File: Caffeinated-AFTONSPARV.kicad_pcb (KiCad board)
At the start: 4 copper layers, 42.5 x 16.1 mm, 37 parts, among them J1 PWR, J2 LED, J3 TagConnect, J4 USB, Q1 AO3400A, Q2 AO3400A, Q3 AO3400A, SW1 SW_Push, U1 ESP32-C3-MINI-1-[H/N]4, U2 SY8201ABC

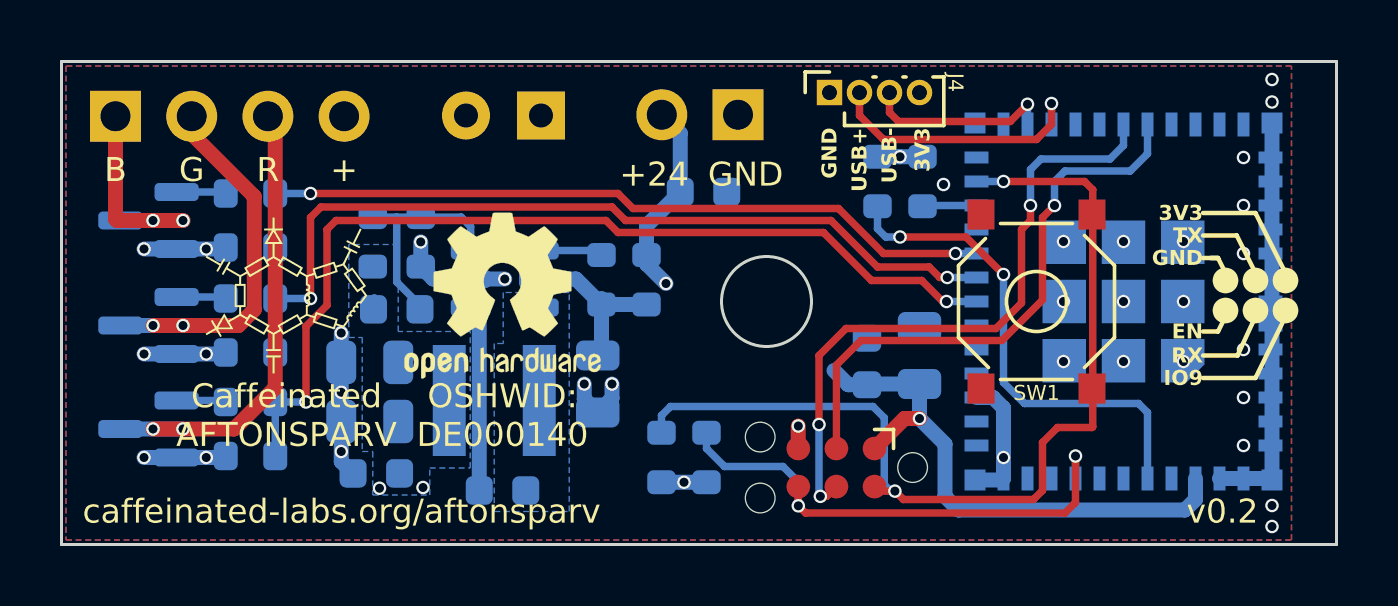
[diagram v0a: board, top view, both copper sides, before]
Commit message: optimize bom for jlcpcb basic parts
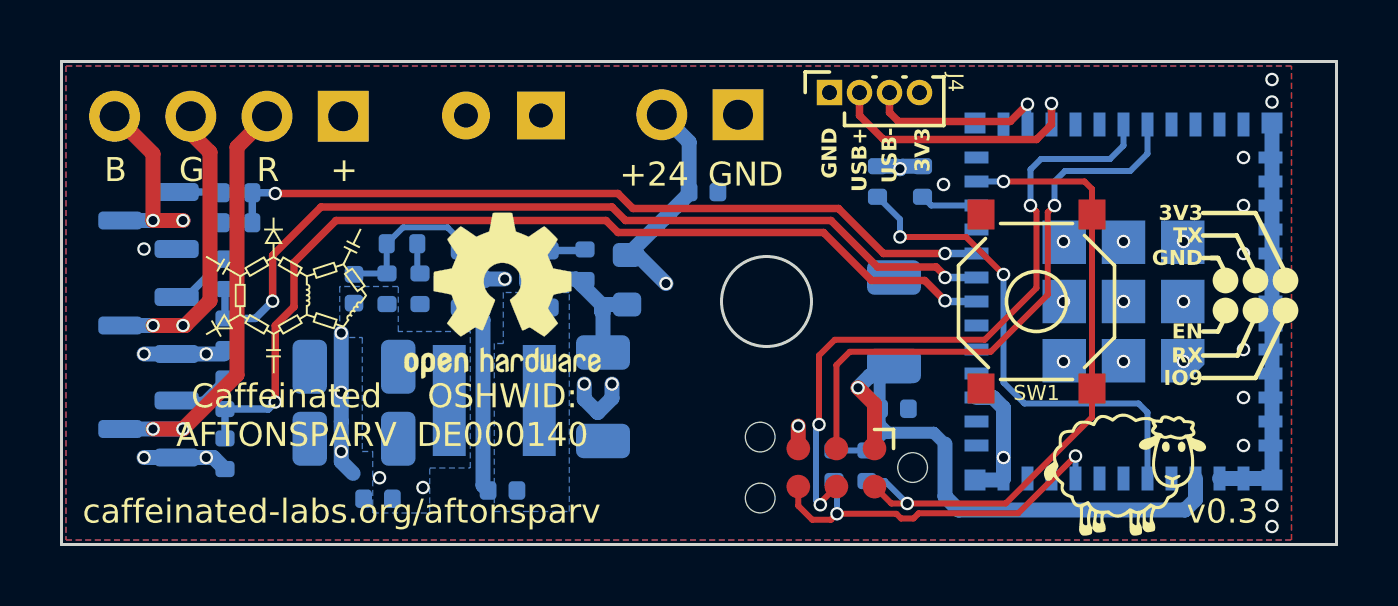
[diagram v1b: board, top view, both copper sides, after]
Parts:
- added R15: 100Ω, Resistor_SMD:R_0402_1005Metric, B.Cu at (141.8, 99.6)
- added sheep: LOGO, LOGO, F.Cu at (165.2, 105.8)
- C1: value 100nF -> 100nF 50V; footprint Capacitor_SMD:C_0603_1608Metric -> Capacitor_SMD:C_0402_1005Metric
- C10, C3, C6, C9: footprint Capacitor_SMD:C_0805_2012Metric -> Capacitor_SMD:C_1206_3216Metric
- C11, C4, C5, C7: footprint Capacitor_SMD:C_0603_1608Metric -> Capacitor_SMD:C_0402_1005Metric
- R1, R10, R12, R14, R2, R3, R7, R8, R9: footprint Resistor_SMD:R_0603_1608Metric -> Resistor_SMD:R_0402_1005Metric
- R13: value 22.1kΩ -> 22kΩ; footprint Resistor_SMD:R_0603_1608Metric -> Resistor_SMD:R_0402_1005Metric
- R4, R5, R6: value 20Ω -> 22Ω; footprint Resistor_SMD:R_0603_1608Metric -> Resistor_SMD:R_0402_1005Metric
- moved J2 7.59 mm to (139.2, 93.8), turned to 90 degrees
- moved R7 6.86 mm to (156.7, 105.5), turned to -90 degrees
- moved R10 4.26 mm to (155.6, 105.5), turned to -90 degrees
- moved C7 1.81 mm to (157.6, 103.6), turned to 0 degrees
- moved R12 1.63 mm to (140.7, 99.6)
- moved C5 1.58 mm to (139.6, 99.6), turned to -90 degrees
- moved C6 1.41 mm to (157.6, 100.7)
- moved R4 1.18 mm to (135.2, 99.1), turned to 90 degrees
- moved R2 1.06 mm to (135.2, 101.1), turned to -90 degrees
- moved R1 0.94 mm to (135.7, 97.4)
- moved R6 0.89 mm to (135.2, 103.1), turned to 90 degrees
- moved R3 0.85 mm to (135.2, 105.1), turned to -90 degrees
- moved C11 0.85 mm to (140.3, 106.6)
- moved C10 0.78 mm to (139.6, 104.6)
- moved R14 0.74 mm to (147.2, 98.8)
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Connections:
- J2 pad 1: Net-(J2-Pin_1) -> +24V
- J2 pad 4: +24V -> Net-(J2-Pin_4)
- Q1 pad 3: Net-(J2-Pin_3) -> Net-(J2-Pin_2)
- Q2 pad 3: Net-(J2-Pin_2) -> Net-(J2-Pin_3)
- Q3 pad 3: Net-(J2-Pin_1) -> Net-(J2-Pin_4)
- R13 pad 2: GND -> Net-(R13-Pad2)
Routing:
- net IO9: track 32.2 -> 21.9 mm
- net Net-(J2-Pin_1): track 7.78 -> 0.00 mm, vias 2 -> 0
- net Net-(J2-Pin_4): track 0.00 -> 7.08 mm, vias 0 -> 2
- net Net-(J2-Pin_3): track 15.9 -> 10.7 mm
- net GND: track 37.9 -> 33.6 mm, vias 36 -> 34
- net EN: track 17.3 -> 13.0 mm
- net +3.3V: track 21.3 -> 23.5 mm, vias 5 -> 4
- net Net-(U2-FB): track 7.54 -> 5.45 mm
- net Net-(J2-Pin_2): track 13.0 -> 14.7 mm
- net Net-(U2-IN): track 5.89 -> 4.86 mm
- net Net-(R13-Pad2): track 0.00 -> 1.03 mm
- net +24V: track 6.61 -> 7.62 mm
- net Net-(U2-EN): track 2.15 -> 1.55 mm
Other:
- board text added: "v0.3"
- board text removed: "v0.2"
